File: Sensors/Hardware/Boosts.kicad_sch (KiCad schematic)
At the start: 38 parts, among them IC1 AP2205-W5-7, IC2 AP2205-W5-7, U11 TPS61092RSAR, U12 LM2623QNHLRQ1

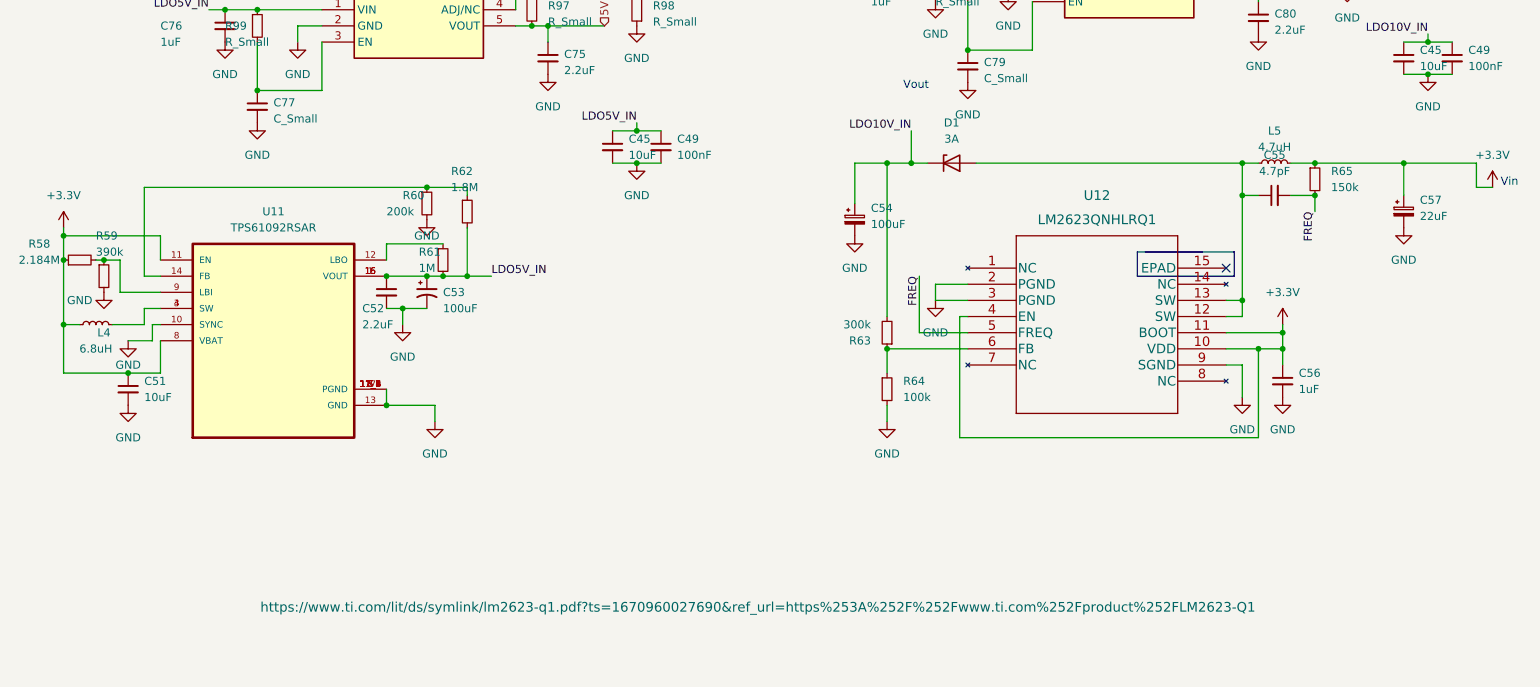
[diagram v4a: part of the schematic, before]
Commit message: Schematic update
unfinished
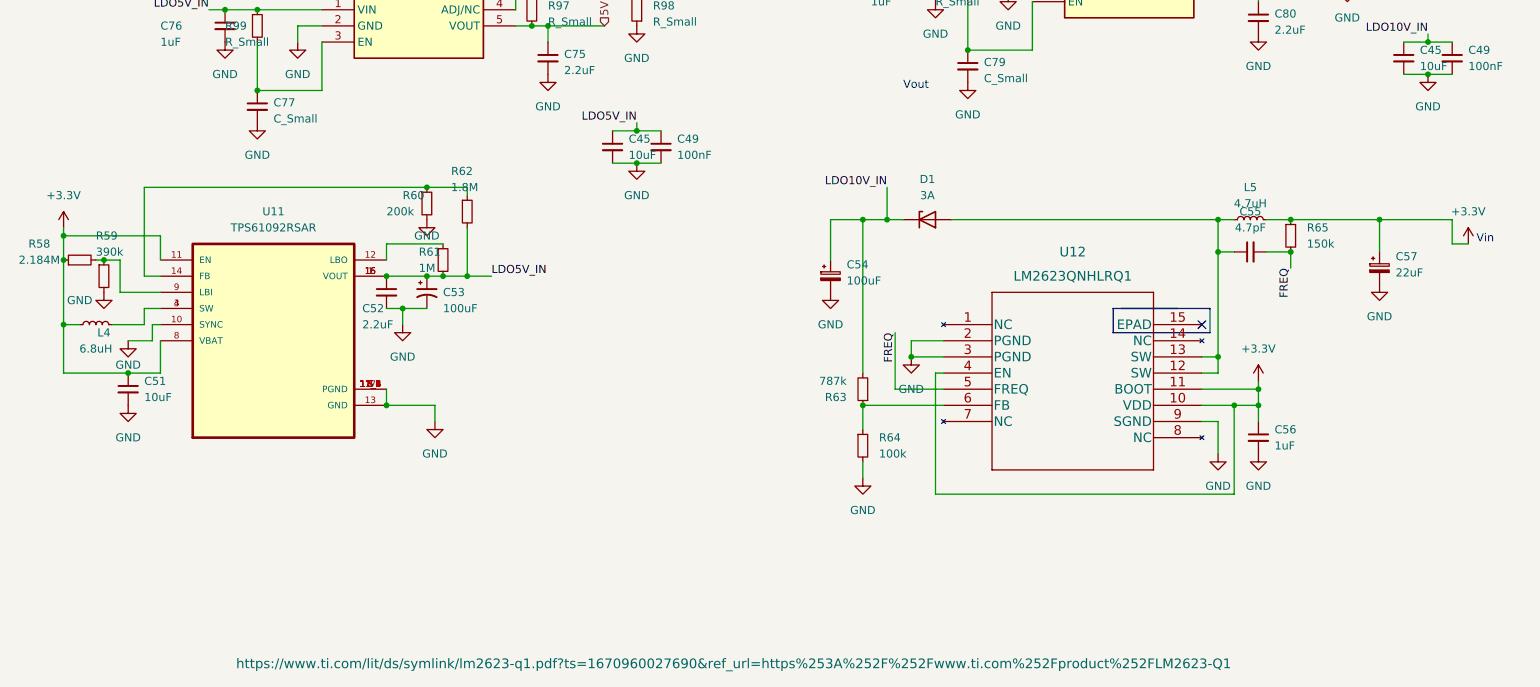
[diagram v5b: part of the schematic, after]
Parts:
- R63: value 300k -> 787k
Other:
- moved on the sheet: C54, C55, C56, C57, D1, L5, R63, R64, R65, U12

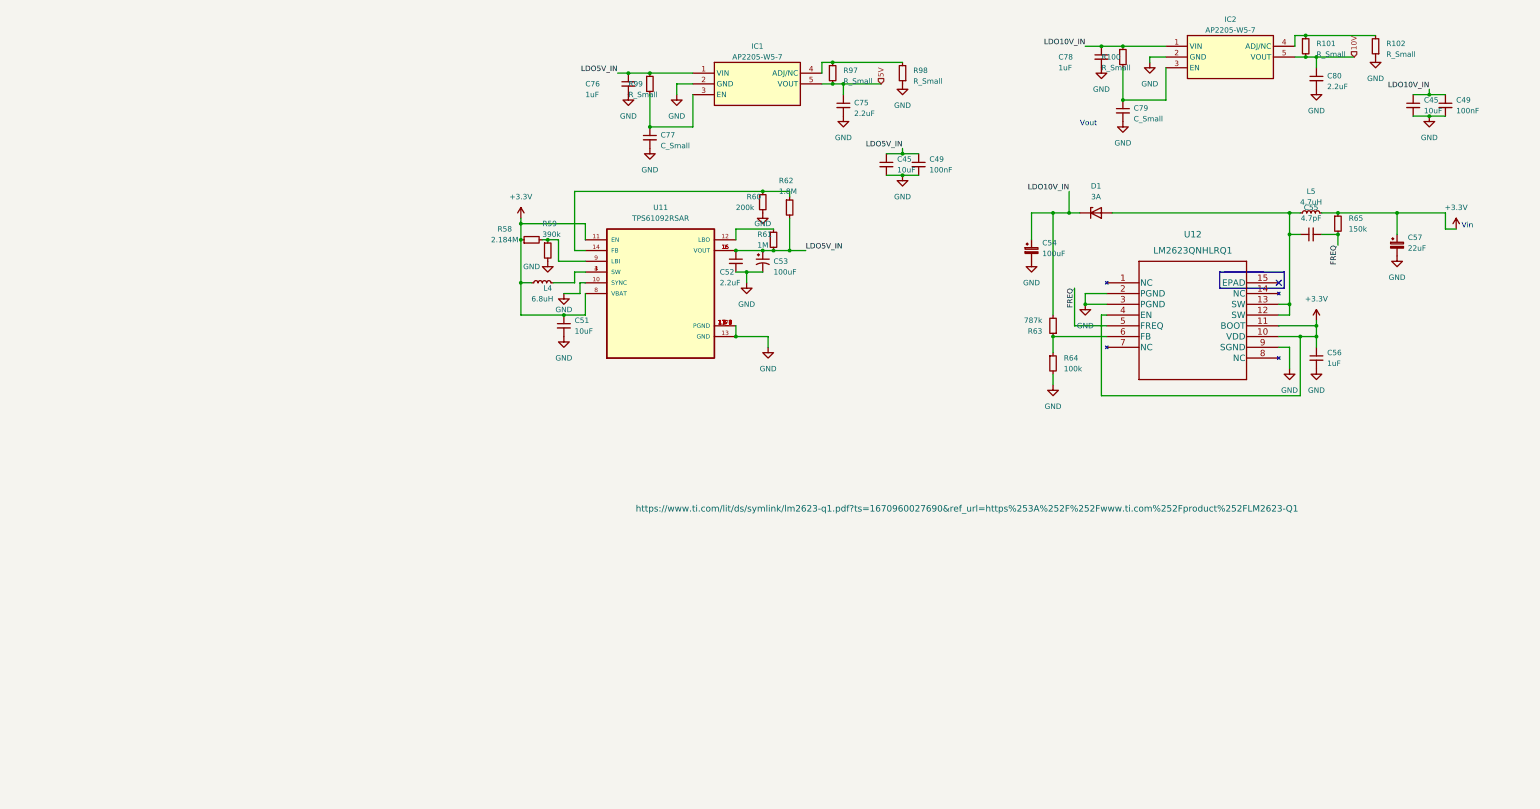
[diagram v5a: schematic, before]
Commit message: changes to schematic
added in components for the layout
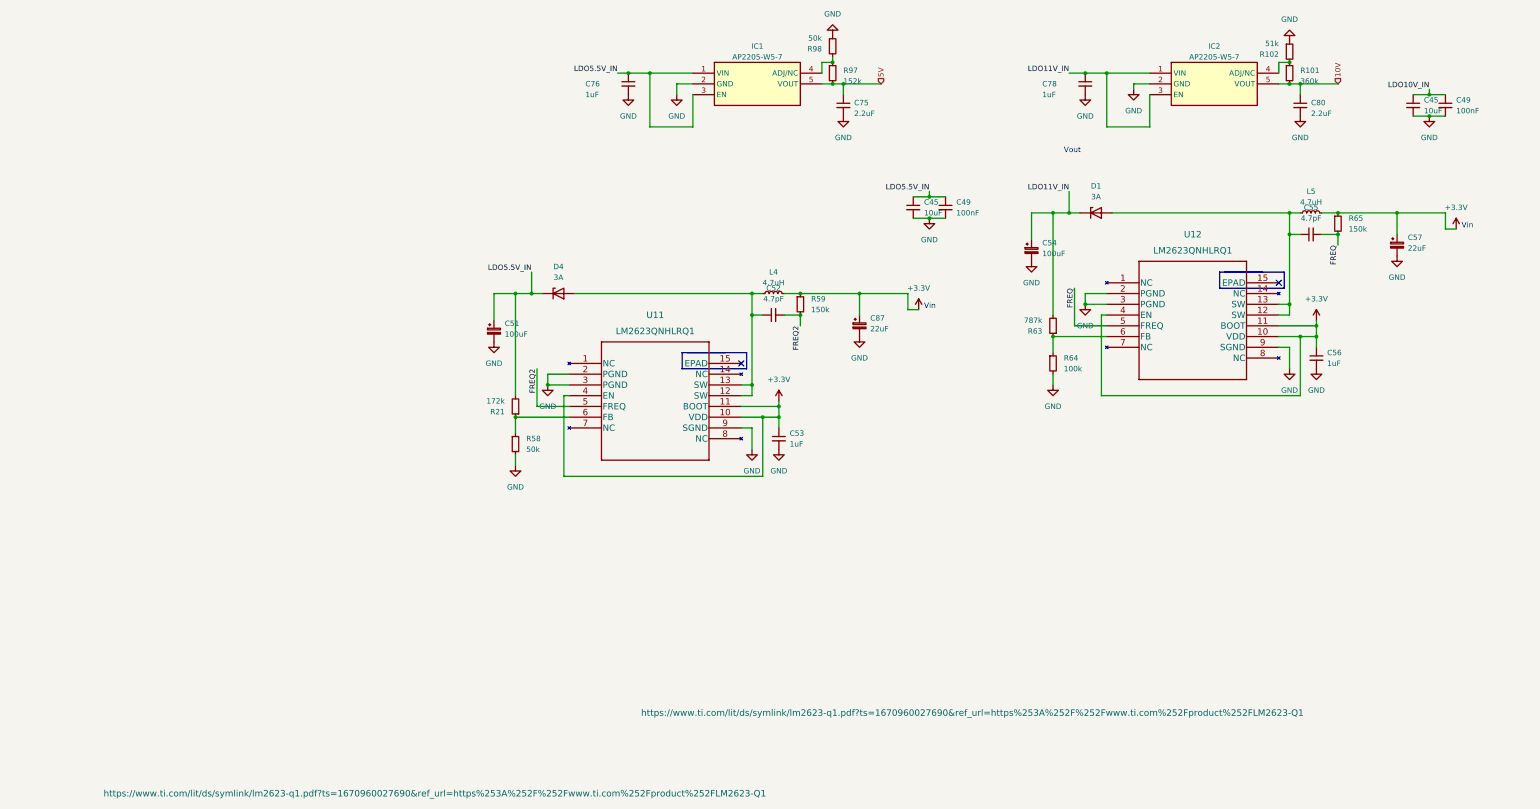
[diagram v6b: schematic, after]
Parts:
- removed C51: 10uF, Capacitor_SMD:C_0603_1608Metric, symbol Device:C_Small
- removed C53: 100uF, iclr:CAPC2012X145N, symbol Device:C_Polarized_Small_US
- removed C77, C79: C_Small, Capacitor_SMD:C_0402_1005Metric, symbol Device:C_Small
- removed R100, R99: R_Small, Resistor_SMD:R_0402_1005Metric, symbol Device:R_Small
- removed R60: 200k, Resistor_SMD:R_0603_1608Metric, symbol Device:R_Small
- removed R61: 1M, Resistor_SMD:R_0603_1608Metric, symbol Device:R_Small
- removed R62: 1.8M, Resistor_SMD:R_0603_1608Metric, symbol Device:R_Small
- removed U11: TPS61092RSAR, iclr:QFN65P400X400X100-17N, symbol iclr:TPS61092RSAR
- added C51: 100uF, Capacitor_SMD:C_0603_1608Metric, symbol Device:C_Polarized_Small
- added C53: 1uF, Capacitor_SMD:C_0402_1005Metric, symbol Device:C_Small
- added C87: 22uF, Capacitor_SMD:C_0603_1608Metric, symbol Device:C_Polarized_Small
- added D4: 3A, Diode_SMD:D_0603_1608Metric, symbol Device:D_Zener
- added R21: 172k, Resistor_SMD:R_0402_1005Metric, symbol Device:R_Small
- added U11: LM2623QNHLRQ1, iclr:LM2623QNHLRQ1, symbol iclr:LM2623QNHLRQ1
- C52: value 2.2uF -> 4.7pF; footprint Capacitor_SMD:C_0603_1608Metric -> Capacitor_SMD:C_0402_1005Metric
- L4: value 6.8uH -> 4.7uH; footprint iclr:INDPM3030X200N -> Inductor_SMD:L_0603_1608Metric
- R101: value R_Small -> 360k
- R102: value R_Small -> 51k
- R58: value 2.184M -> 50k; footprint Resistor_SMD:R_0603_1608Metric -> Resistor_SMD:R_0402_1005Metric
- R59: value 390k -> 150k; footprint Resistor_SMD:R_0603_1608Metric -> Resistor_SMD:R_0402_1005Metric
- R97: value R_Small -> 152k; footprint Resistor_SMD:R_0402_1005Metric -> Resistor_SMD:R_0603_1608Metric
- R98: value R_Small -> 50k
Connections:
- net +3V3: now also L4.2, R59.1, C53.1, C87.1, U11.10 (VDD), U11.11 (BOOT), U11.4 (EN); no longer L4.1, R58.1
- net GND: now also R58.2, C51.2, C53.2, C87.2, U11.2 (PGND), U11.3 (PGND), U11.9 (SGND); no longer C52.2, R59.2
- net LDO10V_IN: no longer C54.1, C78.1, D1.1 (K), IC2.1 (VIN), R63.2
- net LDO11V_IN: now reaches IC2.3 (EN)
- net LDO11V_IN: now also C54.1, C78.1, D1.1 (K), IC2.1 (VIN), R63.2
- net LDO5.5V_IN: now reaches IC1.3 (EN)
- net LDO5.5V_IN: now also C45.1, C49.1, C76.1, IC1.1 (VIN), C51.1, D4.1 (K), R21.2
- removed net LDO5V_IN: C45.1, C49.1, C52.1, C76.1, IC1.1 (VIN)
- new net: C52.1, D4.2 (A), L4.1, U11.12 (SW), U11.13 (SW)
- new net: R21.1, R58.1, U11.6 (FB)
- new net FREQ2: C52.2, R59.2, U11.5 (FREQ)
- no-connect marks 1 -> 2
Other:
- moved on the sheet: C45, C49, C78, C80, IC2, R101, R102, R98

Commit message: Power sorted
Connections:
- net LDO10V_IN is gone; now on net LDO11V_IN: C45.1, C49.1
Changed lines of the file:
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@@
     (effects (font (size 1.27 1.27)) (justify left bottom))
   )
-  (label "LDO10V_IN" (at 264.16 34.29 180) (fields_autoplaced)
+  (label "LDO11V_IN" (at 264.16 34.29 180) (fields_autoplaced)
     (effects (font (size 1.27 1.27)) (justify right bottom))
   )

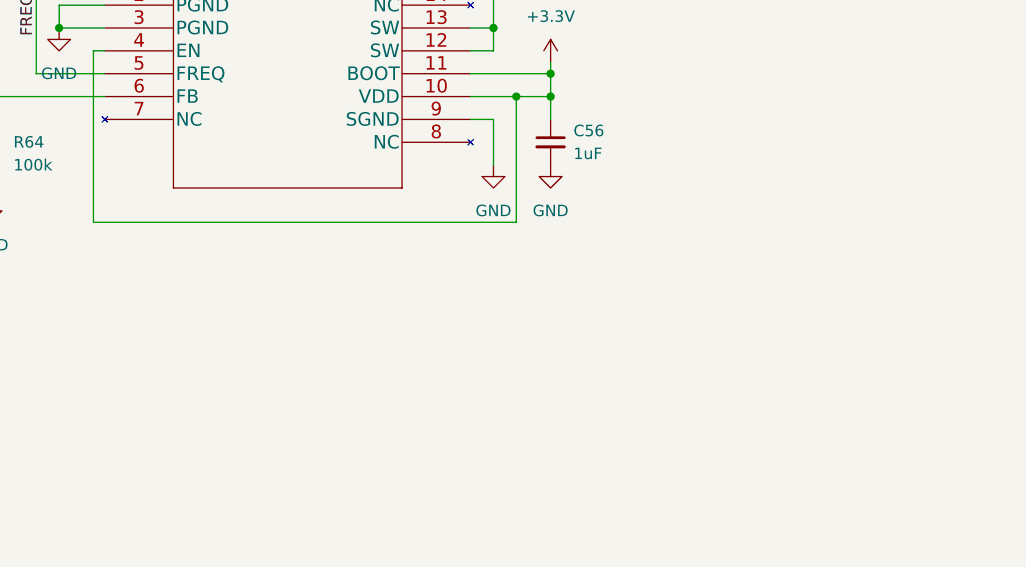
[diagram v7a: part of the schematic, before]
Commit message: optimised the boost layouts
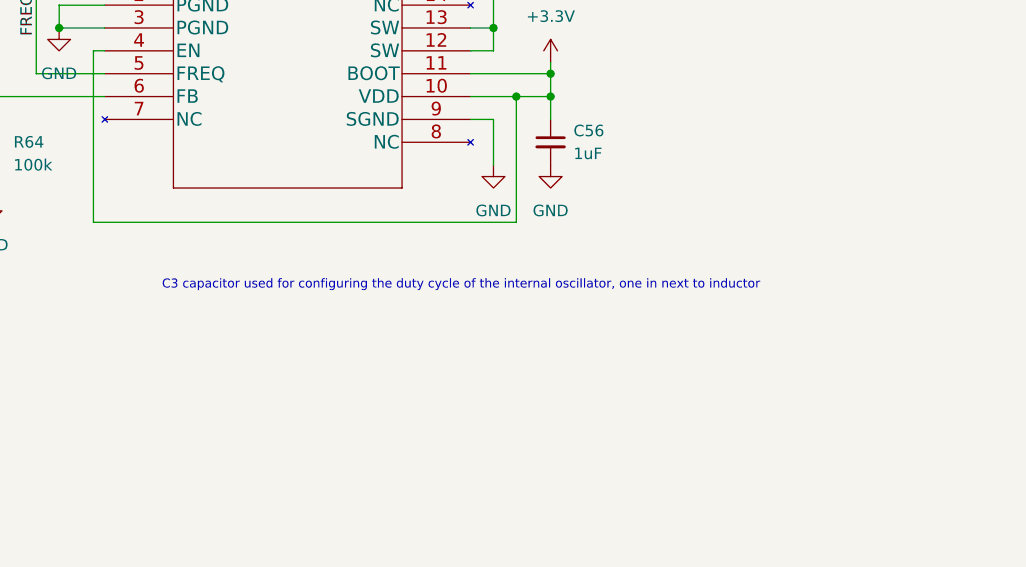
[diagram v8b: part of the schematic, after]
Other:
- note added: "C3 capacitor used for configuring the duty cycle of the internal oscillator, one in next to inductor"
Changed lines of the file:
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@@
     (effects (font (size 1.27 1.27)) (justify left bottom))
+  )
+  (text "C3 capacitor used for configuring the duty cycle of the internal oscillator, one in next to inductor\n"
+    (at 194.31 114.3 0)
+    (effects (font (size 1 1)) (justify left bottom))
   )
   (text "Vin" (at 144.78 86.36 0)
